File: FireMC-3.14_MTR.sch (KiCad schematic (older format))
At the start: 24 parts

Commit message: Schematic 80% complete
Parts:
- removed J? (x4): Header_1X3, symbol Header_1X3
- added C?: C, symbol C
- added J?: Header_1X2, symbol Header_1X2
- added R?: 330R, symbol R
- added R?: 3k3, symbol R
- added R?: 100k, symbol R
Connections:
- net EN2: now also R?.1
- net GND: now also C?.2, J?.2, R?.2
- net VCC: now also R?.2
- new net: J?.1, R?.2
- new net ALLSTOP: C?.1, R?.1, R?.1
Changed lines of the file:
@@
 	3300 2800 3500 2800
 Wire Wire Line
-	3000 3600 3300 3600
-Wire Wire Line
-	3300 3600 3300 3700
-Wire Wire Line
-	3300 3700 3500 3700
+	3100 3700 3500 3700
 Wire Wire Line
 	3400 4250 3400 4100
@@
 $EndComp
 $Comp
-L Header_1X3 J?
-U 1 1 57D1A629
-P 3800 7500
-F 0 "J?" H 3800 7750 60  0000 C CNN
-F 1 "Header_1X3" H 3800 7250 60  0000 C CNN
-F 2 "" H 3800 7450 60  0000 C CNN
-F 3 "" H 3800 7450 60  0000 C CNN
-	1    3800 7500
+L Header_1X2 J?
+U 1 1 57D5CF02
+P 1100 5300
+F 0 "J?" H 1100 5500 60  0000 C CNN
+F 1 "Header_1X2" H 1100 5100 60  0000 C CNN
+F 2 "" H 1100 5200 60  0000 C CNN
+F 3 "" H 1100 5200 60  0000 C CNN
+	1    1100 5300
 	-1   0    0    -1
 $EndComp
 $Comp
-L Header_1X3 J?
-U 1 1 57D1A749
-P 2800 7500
-F 0 "J?" H 2800 7750 60  0000 C CNN
-F 1 "Header_1X3" H 2800 7250 60  0000 C CNN
-F 2 "" H 2800 7450 60  0000 C CNN
-F 3 "" H 2800 7450 60  0000 C CNN
-	1    2800 7500
-	-1   0    0    -1
-$EndComp
-$Comp
-L Header_1X3 J?
-U 1 1 57D1A7FF
-P 1800 7500
-F 0 "J?" H 1800 7750 60  0000 C CNN
-F 1 "Header_1X3" H 1800 7250 60  0000 C CNN
-F 2 "" H 1800 7450 60  0000 C CNN
-F 3 "" H 1800 7450 60  0000 C CNN
-	1    1800 7500
-	-1   0    0    -1
-$EndComp
-$Comp
-L Header_1X3 J?
-U 1 1 57D1A87E
-P 800 7500
-F 0 "J?" H 800 7750 60  0000 C CNN
-F 1 "Header_1X3" H 800 7250 60  0000 C CNN
-F 2 "" H 800 7450 60  0000 C CNN
-F 3 "" H 800 7450 60  0000 C CNN
-	1    800  7500
-	-1   0    0    -1
+L R R?
+U 1 1 57D5CF43
+P 1750 5250
+F 0 "R?" V 1830 5250 50  0000 C CNN
+F 1 "330R" V 1750 5250 50  0000 C CNN
+F 2 "" V 1680 5250 50  0000 C CNN
+F 3 "" H 1750 5250 50  0000 C CNN
+	1    1750 5250
+	0    1    1    0
+$EndComp
+$Comp
+L C C?
+U 1 1 57D5CFEE
+P 2300 5500
+F 0 "C?" H 2325 5600 50  0000 L CNN
+F 1 "C" H 2325 5400 50  0000 L CNN
+F 2 "" H 2338 5350 50  0000 C CNN
+F 3 "" H 2300 5500 50  0000 C CNN
+	1    2300 5500
+	1    0    0    -1
 $EndComp
 $Comp
 L GND #PWR?
-U 1 1 57D1AB18
-P 1200 7700
-F 0 "#PWR?" H 1200 7450 50  0001 C CNN
-F 1 "GND" H 1200 7550 50  0000 C CNN
-F 2 "" H 1200 7700 50  0000 C CNN
-F 3 "" H 1200 7700 50  0000 C CNN
-	1    1200 7700
-	1    0    0    -1
-$EndComp
-$Comp
-L GND #PWR?
-U 1 1 57D1AB6B
-P 2200 7700
-F 0 "#PWR?" H 2200 7450 50  0001 C CNN
-F 1 "GND" H 2200 7550 50  0000 C CNN
-F 2 "" H 2200 7700 50  0000 C CNN
-F 3 "" H 2200 7700 50  0000 C CNN
-	1    2200 7700
-	1    0    0    -1
-$EndComp
-$Comp
-L GND #PWR?
-U 1 1 57D1ABBE
-P 3200 7700
-F 0 "#PWR?" H 3200 7450 50  0001 C CNN
-F 1 "GND" H 3200 7550 50  0000 C CNN
-F 2 "" H 3200 7700 50  0000 C CNN
-F 3 "" H 3200 7700 50  0000 C CNN
-	1    3200 7700
-	1    0    0    -1
-$EndComp
-$Comp
-L GND #PWR?
-U 1 1 57D1AC11
-P 4200 7700
-F 0 "#PWR?" H 4200 7450 50  0001 C CNN
-F 1 "GND" H 4200 7550 50  0000 C CNN
-F 2 "" H 4200 7700 50  0000 C CNN
-F 3 "" H 4200 7700 50  0000 C CNN
-	1    4200 7700
-	1    0    0    -1
-$EndComp
-$Comp
-L VCC #PWR?
-U 1 1 57D1AC64
-P 1200 7300
-F 0 "#PWR?" H 1200 7150 50  0001 C CNN
-F 1 "VCC" H 1200 7450 50  0000 C CNN
-F 2 "" H 1200 7300 50  0000 C CNN
-F 3 "" H 1200 7300 50  0000 C CNN
-	1    1200 7300
-	1    0    0    -1
-$EndComp
-$Comp
-L VCC #PWR?
-U 1 1 57D1ACB7
-P 2200 7300
-F 0 "#PWR?" H 2200 7150 50  0001 C CNN
-F 1 "VCC" H 2200 7450 50  0000 C CNN
-F 2 "" H 2200 7300 50  0000 C CNN
-F 3 "" H 2200 7300 50  0000 C CNN
-	1    2200 7300
-	1    0    0    -1
-$EndComp
-$Comp
-L VCC #PWR?
-U 1 1 57D1AD0A
-P 3200 7300
-F 0 "#PWR?" H 3200 7150 50  0001 C CNN
-F 1 "VCC" H 3200 7450 50  0000 C CNN
-F 2 "" H 3200 7300 50  0000 C CNN
-F 3 "" H 3200 7300 50  0000 C CNN
-	1    3200 7300
-	1    0    0    -1
-$EndComp
-$Comp
-L VCC #PWR?
-U 1 1 57D1AD5D
-P 4200 7300
-F 0 "#PWR?" H 4200 7150 50  0001 C CNN
-F 1 "VCC" H 4200 7450 50  0000 C CNN
-F 2 "" H 4200 7300 50  0000 C CNN
-F 3 "" H 4200 7300 50  0000 C CNN
-	1    4200 7300
-	1    0    0    -1
-$EndComp
-Text GLabel 1300 7600 2    50   Input ~ 0
-XMAX
-Text GLabel 2300 7600 2    50   Input ~ 0
-YMAX
-Text GLabel 3300 7600 2    50   Input ~ 0
-ZMAX
-Text GLabel 4300 7600 2    50   Input ~ 0
-EMAX
-Wire Wire Line
-	1100 7400 1200 7400
-Wire Wire Line
-	1200 7400 1200 7300
-Wire Wire Line
-	1100 7500 1200 7500
-Wire Wire Line
-	1200 7500 1200 7700
-Wire Wire Line
-	1100 7600 1300 7600
-Wire Wire Line
-	2100 7400 2200 7400
-Wire Wire Line
-	2200 7400 2200 7300
-Wire Wire Line
-	2100 7500 2200 7500
-Wire Wire Line
-	2200 7500 2200 7700
-Wire Wire Line
-	2100 7600 2300 7600
-Wire Wire Line
-	3100 7600 3300 7600
-Wire Wire Line
-	4100 7600 4300 7600
-Wire Wire Line
-	4200 7700 4200 7500
-Wire Wire Line
-	4200 7500 4100 7500
-Wire Wire Line
-	4100 7400 4200 7400
-Wire Wire Line
-	4200 7400 4200 7300
-Wire Wire Line
-	3200 7700 3200 7500
-Wire Wire Line
-	3200 7500 3100 7500
-Wire Wire Line
-	3100 7400 3200 7400
-Wire Wire Line
-	3200 7400 3200 7300
+U 1 1 57D5D056
+P 1500 5850
+F 0 "#PWR?" H 1500 5600 50  0001 C CNN
+F 1 "GND" H 1500 5700 50  0000 C CNN
+F 2 "" H 1500 5850 50  0000 C CNN
+F 3 "" H 1500 5850 50  0000 C CNN
+	1    1500 5850
+	1    0    0    -1
+$EndComp
+Wire Wire Line
+	1400 5350 1500 5350
+Wire Wire Line
+	1500 5350 1500 5850
+Wire Wire Line
+	1500 5750 2300 5750
+Connection ~ 1500 5750
+Wire Wire Line
+	1900 5250 2300 5250
+Wire Wire Line
+	1600 5250 1400 5250
+Text Label 2250 5250 2    50   ~ 0
+ALLSTOP
+Wire Wire Line
+	2300 5150 2300 5350
+Wire Wire Line
+	2300 5750 2300 5650
+$Comp
+L R R?
+U 1 1 57D5DAD7
+P 2300 5000
+F 0 "R?" V 2380 5000 50  0000 C CNN
+F 1 "3k3" V 2300 5000 50  0000 C CNN
+F 2 "" V 2230 5000 50  0000 C CNN
+F 3 "" H 2300 5000 50  0000 C CNN
+	1    2300 5000
+	-1   0    0    1
+$EndComp
+Connection ~ 2300 5250
+$Comp
+L VCC #PWR?
+U 1 1 57D5DD2E
+P 2300 4750
+F 0 "#PWR?" H 2300 4600 50  0001 C CNN
+F 1 "VCC" H 2300 4900 50  0000 C CNN
+F 2 "" H 2300 4750 50  0000 C CNN
+F 3 "" H 2300 4750 50  0000 C CNN
+	1    2300 4750
+	1    0    0    -1
+$EndComp
+Wire Wire Line
+	2300 4850 2300 4750
+Wire Wire Line
+	3000 3600 3100 3600
+Wire Wire Line
+	3100 3600 3100 3800
+Connection ~ 3100 3700
+$Comp
+L R R?
+U 1 1 57D5E9E3
+P 3100 3950
+F 0 "R?" V 3180 3950 50  0000 C CNN
+F 1 "100k" V 3100 3950 50  0000 C CNN
+F 2 "" V 3030 3950 50  0000 C CNN
+F 3 "" H 3100 3950 50  0000 C CNN
+	1    3100 3950
+	1    0    0    -1
+$EndComp
+Wire Wire Line
+	3100 4100 3100 4200
+Wire Wire Line
+	3100 4200 3400 4200
+Connection ~ 3400 4200
 $EndSCHEMATC

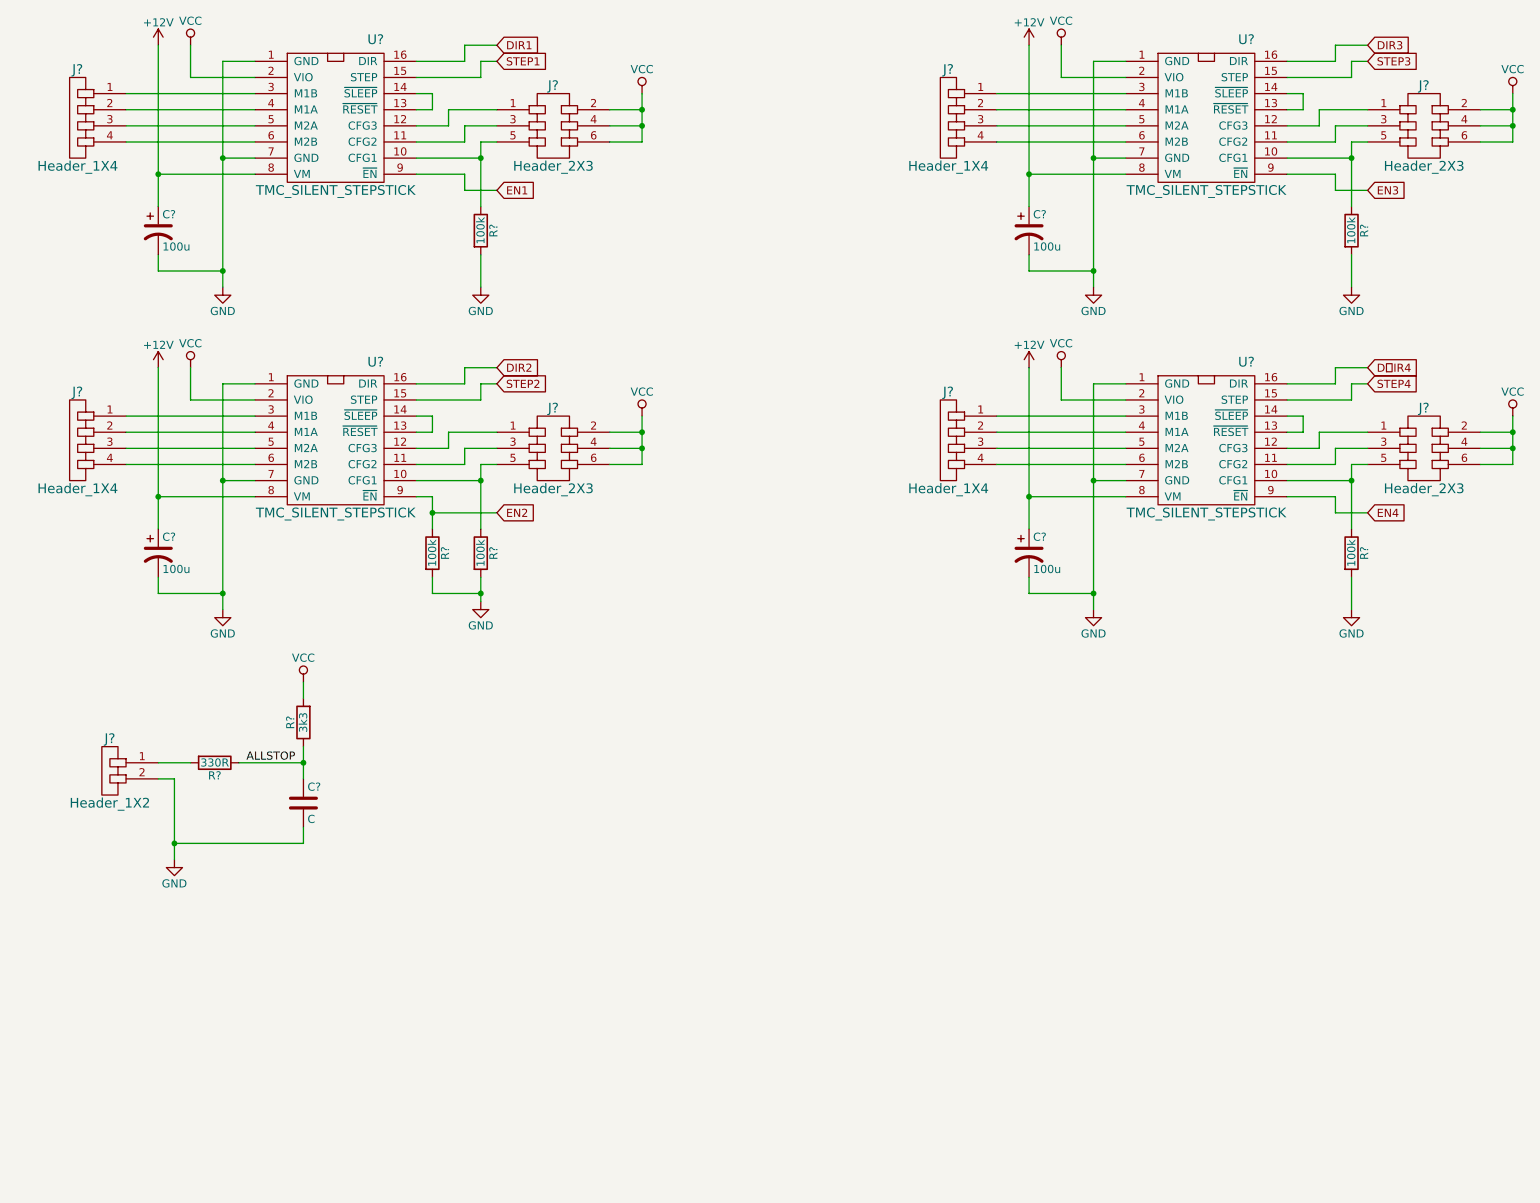
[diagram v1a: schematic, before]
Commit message: Schematic corrections
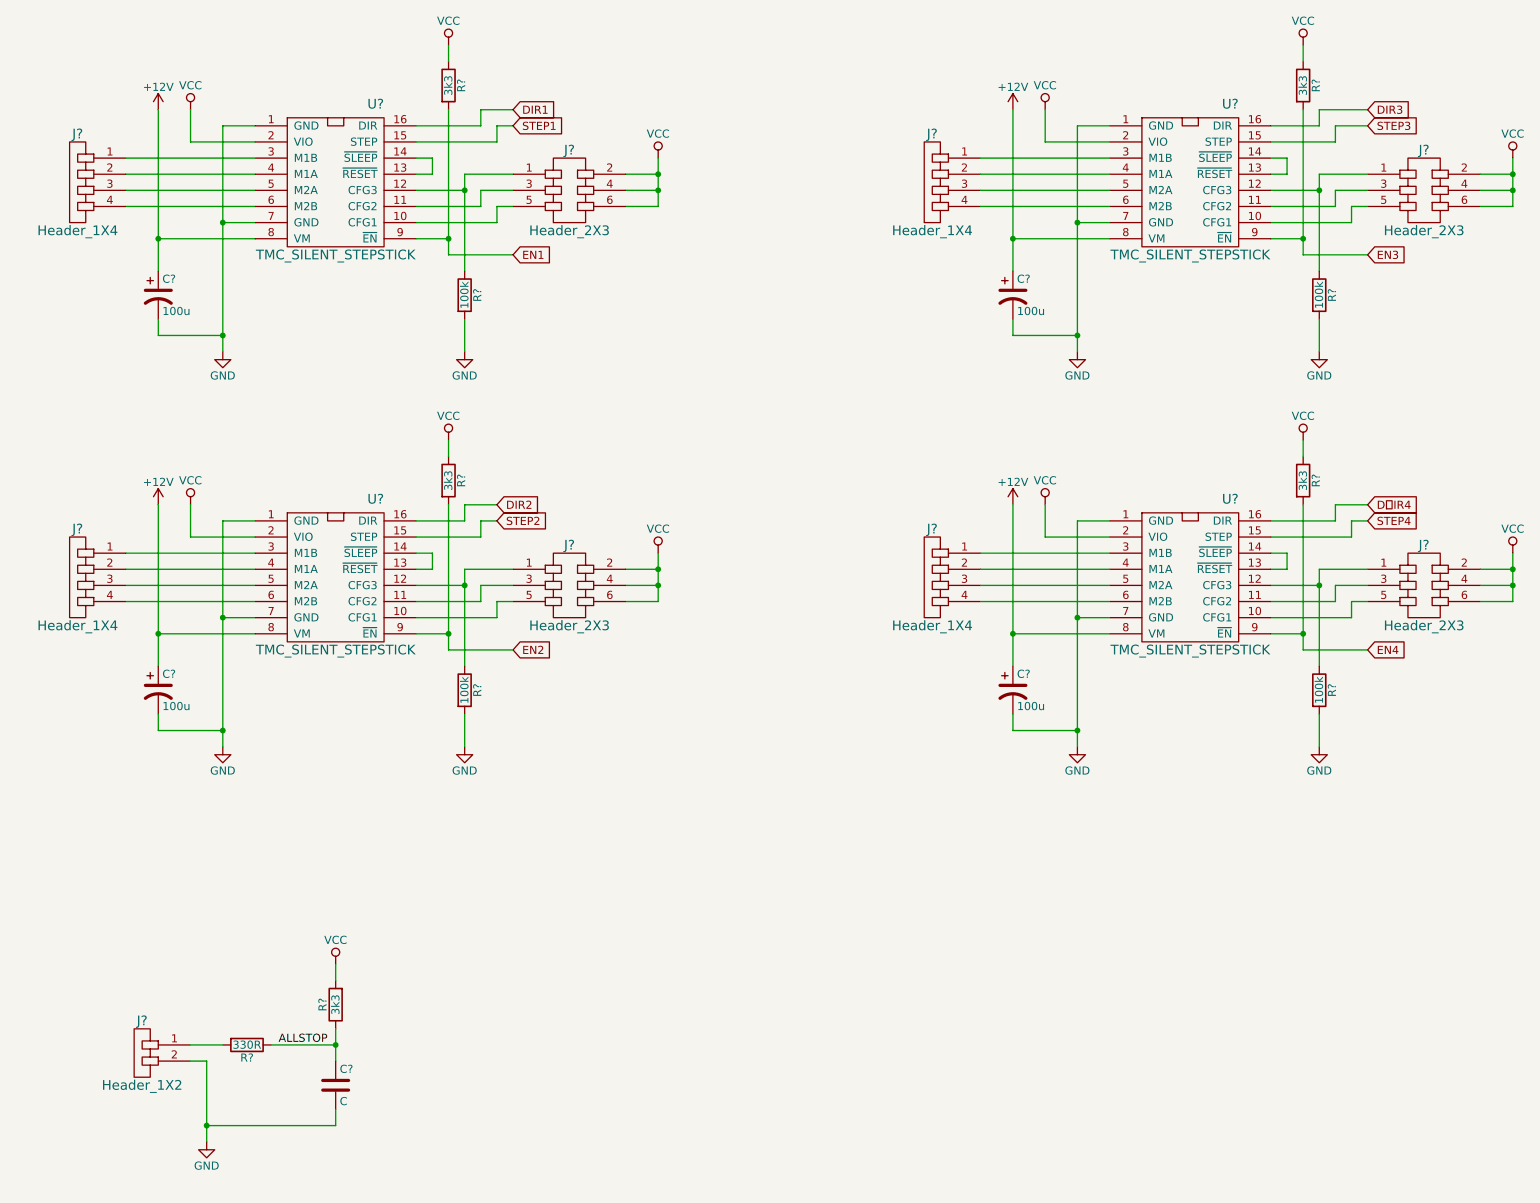
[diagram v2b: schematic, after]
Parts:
- added R? (x3): 3k3, symbol R
- R?: value 100k -> 3k3
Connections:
- net EN1: now also R?.2
- net EN2: now also R?.2; no longer R?.1
- net EN3: now also R?.2
- net EN4: now also R?.2
- net GND: no longer R?.2
- net VCC: now also R?.1, R?.1, R?.1, R?.1
- net at J?.1, U?.12 (CFG3): now also R?.1 (x4)
- net at J?.5, U?.10 (CFG1): no longer R?.1 (x4)
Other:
- moved on the sheet: C?, J?, R?, U?

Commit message: Schematic Complete for full comments
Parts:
- added R? (x4): 100k, symbol R
- added U?: 74AHC1G14, symbol 74AHC1G14
- added U? (x4): 74LS32, symbol 74LS32
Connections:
- net ALLSTOP: now also U?.2
- net EN1: now also U?.1; no longer R?.2, U?.9 (~EN)
- net EN2: now also U?.4; no longer R?.2, U?.9 (~EN)
- net EN3: now also U?.9; no longer R?.2, U?.9 (~EN)
- net EN4: now also U?.12; no longer R?.2, U?.9 (~EN)
- net GND: now also R?.2, R?.2, R?.2, R?.2, U?.3 (GND), U?.7 (GND), U?.7 (GND), U?.7 (GND), U?.7 (GND)
- net VCC: now also U?.14 (VCC), U?.14 (VCC), U?.14 (VCC), U?.14 (VCC), U?.5 (VCC)
- net at J?.5, U?.10 (CFG1): now also R?.1 (x4)
- new net EN1_O: R?.2, U?.3, U?.9 (~EN)
- new net EN2_O: R?.2, U?.6, U?.9 (~EN)
- new net EN3_O: R?.2, U?.8, U?.9 (~EN)
- new net EN4_O: R?.2, U?.11, U?.9 (~EN)
- new net ~ALLSTOP: U?.10, U?.13, U?.2, U?.4, U?.5
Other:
- moved on the sheet: C?, J?, R?

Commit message: PCB Layout experimentation
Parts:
- removed C?: C, symbol C
- removed J?: Header_1X2, symbol Header_1X2
- removed R?: 330R, symbol R
- removed R?: 3k3, symbol R
- removed U?: 74AHC1G14, symbol 74AHC1G14
- removed U? (x4): 74LS32, symbol 74LS32
- C37, C38, C40, C41: renamed from C?; footprint (none) -> IPC_CAP:CAPAE840X650N
- J10, J11, J6, J7: renamed from J?; footprint (none) -> IPC_MFG:TE_5-146254-3
- J3, J4, J8, J9: renamed from J?; footprint (none) -> IPC_MFG:SULLINS_PRPC004SAAN-RC
- R17, R18, R19, R20, R21, R22, R23, R24, R25, R26, R27, R28: renamed from R?; footprint (none) -> IPC_RES:RESC1608X55N
- U3, U4, U7, U8: renamed from U?; footprint (none) -> IPC_MFG:stepstick
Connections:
- net DIR4 renamed DIR4
